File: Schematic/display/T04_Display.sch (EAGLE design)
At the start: 46 parts

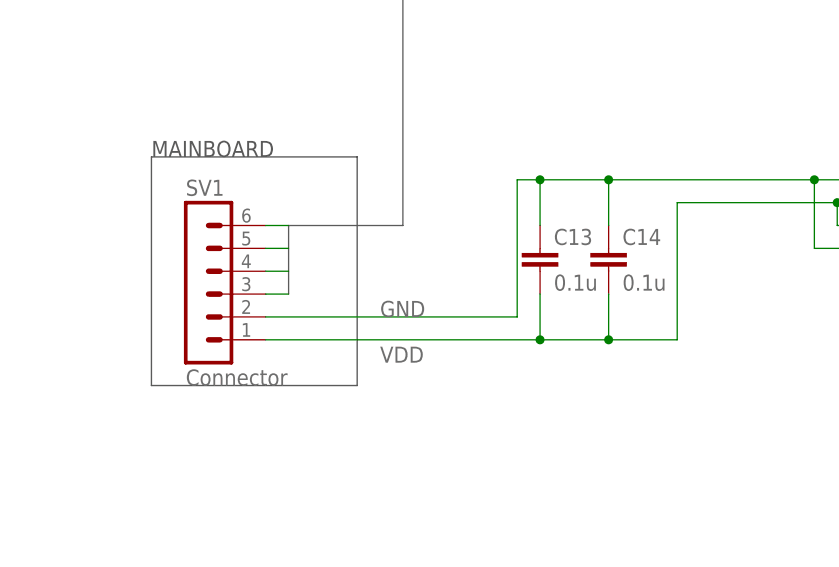
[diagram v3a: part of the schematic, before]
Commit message: Mainboard & Display layout updates - Molex connectors, Mounting Holes, Greenberg Email Additions
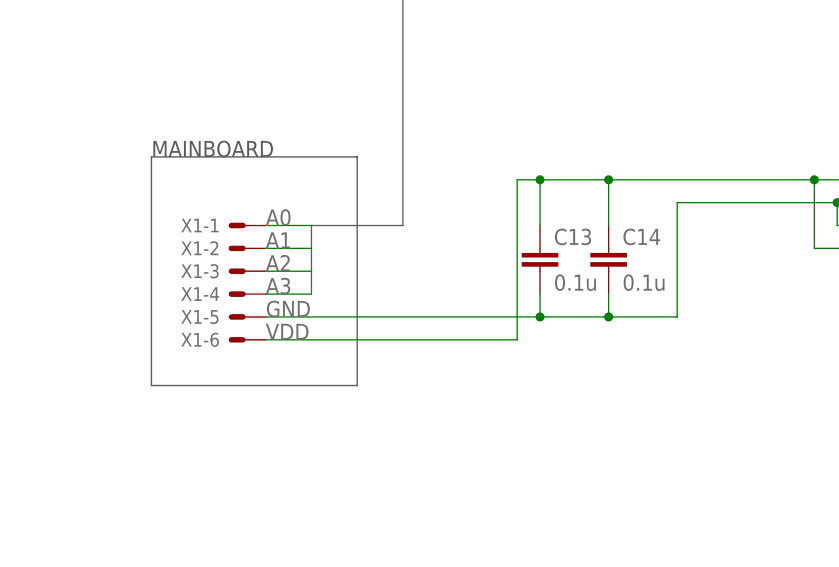
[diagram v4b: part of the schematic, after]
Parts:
- removed SV1: Connector, con-lstb:MA06-1
- added X1: (no value), con-molex:22-23-2061
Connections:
- net A0: now also X1-1.S; no longer SV1.6
- net A1: now also X1-2.S; no longer SV1.5
- net A2: now also X1-3.S; no longer SV1.4
- net A3: now also X1-4.S; no longer SV1.3
- net GND: now also X1-6.S; no longer SV1.2
- net VDD: now also X1-5.S; no longer SV1.1
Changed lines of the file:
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@@
 <parts>
 <part name="FRAME1" library="frames" deviceset="FRAME_B_L" device=""/>
-<part name="SV1" library="con-lstb" deviceset="MA06-1" device="" value="Connector"/>
 <part name="U$1" library="display" deviceset="2N7002" device=""/>
 <part name="REAR" library="display" deviceset="CD4043" device=""/>
@@
 <part name="R8" library="rcl" deviceset="R-US_" device="R1206" value="150"/>
 <part name="R9" library="rcl" deviceset="R-US_" device="R1206" value="150"/>
+<part name="X1" library="con-molex" deviceset="22-23-2061" device=""/>
 </parts>
 <sheets>
@@
 <instance part="FRAME1" gate="G$1" x="0" y="0"/>
 <instance part="FRAME1" gate="G$2" x="325.12" y="0"/>
-<instance part="SV1" gate="1" x="55.88" y="63.5"/>
 <instance part="U$1" gate="G$1" x="299.72" y="248.92"/>
 <instance part="REAR" gate="G$1" x="254" y="200.66"/>
@@
 <instance part="R8" gate="G$1" x="335.28" y="124.46" rot="R90"/>
 <instance part="R9" gate="G$1" x="299.72" y="124.46" rot="R90"/>
+<instance part="X1" gate="-1" x="60.96" y="68.58" rot="MR0"/>
+<instance part="X1" gate="-2" x="60.96" y="66.04" rot="MR0"/>
+<instance part="X1" gate="-3" x="60.96" y="63.5" rot="MR0"/>
+<instance part="X1" gate="-4" x="60.96" y="60.96" rot="MR0"/>
+<instance part="X1" gate="-5" x="60.96" y="58.42" rot="MR0"/>
+<instance part="X1" gate="-6" x="60.96" y="55.88" rot="MR0"/>
 </instances>
 <busses>
@@
 <bus name="A0,A1,A2,A3">
 <segment>
-<wire x1="66.04" y1="60.96" x2="66.04" y2="68.58" width="0.762" layer="92"/>
-<wire x1="66.04" y1="68.58" x2="78.74" y2="68.58" width="0.762" layer="92"/>
+<wire x1="68.58" y1="60.96" x2="68.58" y2="68.58" width="0.762" layer="92"/>
+<wire x1="68.58" y1="68.58" x2="78.74" y2="68.58" width="0.762" layer="92"/>
 <wire x1="78.74" y1="68.58" x2="78.74" y2="99.06" width="0.762" layer="92"/>
 <wire x1="78.74" y1="99.06" x2="127" y2="99.06" width="0.762" layer="92"/>
@@
 </segment>
 <segment>
-<pinref part="SV1" gate="1" pin="2"/>
-<wire x1="63.5" y1="58.42" x2="91.44" y2="58.42" width="0.1524" layer="91"/>
-<wire x1="91.44" y1="58.42" x2="91.44" y2="73.66" width="0.1524" layer="91"/>
+<wire x1="91.44" y1="55.88" x2="91.44" y2="73.66" width="0.1524" layer="91"/>
 <pinref part="U$3" gate="G$1" pin="VSS"/>
 <wire x1="91.44" y1="73.66" x2="93.98" y2="73.66" width="0.1524" layer="91"/>
-<label x="76.2" y="58.42" size="1.778" layer="95"/>
+<label x="63.5" y="58.42" size="1.778" layer="95"/>
 <junction x="124.46" y="73.66"/>
 <wire x1="93.98" y1="73.66" x2="101.6" y2="73.66" width="0.1524" layer="91"/>
@@
 <wire x1="101.6" y1="68.58" x2="101.6" y2="73.66" width="0.1524" layer="91"/>
 <junction x="101.6" y="73.66"/>
+<pinref part="X1" gate="-6" pin="S"/>
+<wire x1="91.44" y1="55.88" x2="63.5" y2="55.88" width="0.1524" layer="91"/>
 </segment>
 </net>
@@
 </segment>
 <segment>
-<pinref part="SV1" gate="1" pin="1"/>
-<wire x1="63.5" y1="55.88" x2="93.98" y2="55.88" width="0.1524" layer="91"/>
-<wire x1="93.98" y1="55.88" x2="101.6" y2="55.88" width="0.1524" layer="91"/>
-<wire x1="101.6" y1="55.88" x2="109.22" y2="55.88" width="0.1524" layer="91"/>
-<wire x1="109.22" y1="55.88" x2="109.22" y2="71.12" width="0.1524" layer="91"/>
+<wire x1="93.98" y1="58.42" x2="101.6" y2="58.42" width="0.1524" layer="91"/>
+<wire x1="101.6" y1="58.42" x2="109.22" y2="58.42" width="0.1524" layer="91"/>
+<wire x1="109.22" y1="58.42" x2="109.22" y2="71.12" width="0.1524" layer="91"/>
 <pinref part="U$3" gate="G$1" pin="VDD"/>
 <wire x1="109.22" y1="71.12" x2="127" y2="71.12" width="0.1524" layer="91"/>
-<label x="76.2" y="53.34" size="1.778" layer="95"/>
+<label x="63.5" y="55.88" size="1.778" layer="95"/>
 <junction x="127" y="71.12"/>
 <wire x1="127" y1="71.12" x2="129.54" y2="71.12" width="0.1524" layer="91"/>
@@
 <wire x1="129.54" y1="68.58" x2="127" y2="68.58" width="0.1524" layer="91"/>
 <wire x1="127" y1="68.58" x2="127" y2="71.12" width="0.1524" layer="91"/>
-<junction x="93.98" y="55.88"/>
-<junction x="101.6" y="55.88"/>
+<junction x="101.6" y="58.42"/>
 <pinref part="C13" gate="G$1" pin="2"/>
-<wire x1="93.98" y1="60.96" x2="93.98" y2="55.88" width="0.1524" layer="91"/>
+<wire x1="93.98" y1="60.96" x2="93.98" y2="58.42" width="0.1524" layer="91"/>
 <pinref part="C14" gate="G$1" pin="2"/>
-<wire x1="101.6" y1="60.96" x2="101.6" y2="55.88" width="0.1524" layer="91"/>
+<wire x1="101.6" y1="60.96" x2="101.6" y2="58.42" width="0.1524" layer="91"/>
+<pinref part="X1" gate="-5" pin="S"/>
+<wire x1="93.98" y1="58.42" x2="63.5" y2="58.42" width="0.1524" layer="91"/>
+<junction x="93.98" y="58.42"/>
 </segment>
 </net>
@@
 </segment>
 <segment>
-<pinref part="SV1" gate="1" pin="6"/>
-<wire x1="66.04" y1="68.58" x2="63.5" y2="68.58" width="0.1524" layer="91"/>
+<wire x1="68.58" y1="68.58" x2="63.5" y2="68.58" width="0.1524" layer="91"/>
+<pinref part="X1" gate="-1" pin="S"/>
+<label x="63.5" y="68.58" size="1.778" layer="95"/>
 </segment>
 </net>
@@
 </segment>
 <segment>
-<pinref part="SV1" gate="1" pin="5"/>
-<wire x1="66.04" y1="66.04" x2="63.5" y2="66.04" width="0.1524" layer="91"/>
+<wire x1="68.58" y1="66.04" x2="63.5" y2="66.04" width="0.1524" layer="91"/>
+<pinref part="X1" gate="-2" pin="S"/>
+<label x="63.5" y="66.04" size="1.778" layer="95"/>
 </segment>
 </net>
@@
 </segment>
 <segment>
-<pinref part="SV1" gate="1" pin="4"/>
-<wire x1="66.04" y1="63.5" x2="63.5" y2="63.5" width="0.1524" layer="91"/>
+<wire x1="68.58" y1="63.5" x2="63.5" y2="63.5" width="0.1524" layer="91"/>
+<pinref part="X1" gate="-3" pin="S"/>
+<label x="63.5" y="63.5" size="1.778" layer="95"/>
 </segment>
 </net>
@@
 </segment>
 <segment>
-<pinref part="SV1" gate="1" pin="3"/>
-<wire x1="66.04" y1="60.96" x2="63.5" y2="60.96" width="0.1524" layer="91"/>
-</segment>
-</net>
+<wire x1="68.58" y1="60.96" x2="63.5" y2="60.96" width="0.1524" layer="91"/>
+<pinref part="X1" gate="-4" pin="S"/>
+<label x="63.5" y="60.96" size="1.778" layer="95"/>
+</segment>
+</net>

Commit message: Updated Schematic and Revision text to match instructor review.
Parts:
- removed C14: 0.1u, resistor:C-EUC1206
- added R10, R11, R12, R13, R14, R15, R16, R17, R18, R19, R20, R21: 4700, rcl:R-US_R1206
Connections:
- removed net N$11: R7.2, U$9.S
- removed net N$2: R8.2, U$8.S
- removed net N$7: R9.2, U$6.S
- new net N$21: LED6.C, U$9.D
- new net N$22: LED4.C, U$6.D
- new net N$23: LED5.C, U$8.D
- net BRES: now also R18.2
- net BS1: now also R21.2
- net BS2: now also R20.2
- net BS3: now also R19.2
- net GND: now also R10.1, R11.1, R12.1, R13.1, R14.1, R15.1, R16.1, R17.1, R18.1, R19.1, R20.1, R21.1, U$1.S, U$10.S, U$12.S, U$13.S, U$4.S, U$5.S, U$6.S, U$8.S, U$9.S; no longer C14.1, LED1.C, LED2.C, LED3.C, LED4.C, LED5.C, LED6.C, LED7.C, LED8.C, LED9.C
- net LRES: now also R14.2
- net LS1: now also R17.2
- net LS2: now also R16.2
- net LS3: now also R15.2
- net N$1: now also LED3.C, U$5.D; no longer R5.2, U$4.S
- net N$13: now also LED7.C, U$10.D; no longer R1.2, U$10.S
- net N$15: now also LED8.C, U$12.D; no longer R2.2, U$12.S
- net N$17: now also LED9.C, U$13.D; no longer R3.2, U$13.S
- net N$3: now also LED2.C, U$4.D; no longer R6.2, U$5.S
- net N$4: now also LED1.C, U$1.D; no longer R4.2, U$1.S
- net RRES: now also R13.2
- net RS1: now also R10.2
- net RS2: now also R11.2
- net RS3: now also R12.2
- net VDD: now also R1.2, R2.2, R3.2, R4.2, R5.2, R6.2, R7.2, R8.2, R9.2; no longer C14.2, U$1.D, U$10.D, U$12.D, U$13.D, U$4.D, U$5.D, U$6.D, U$8.D, U$9.D
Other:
- note added: "1.2"
- note removed: "1.1"
- moved on the sheet: LED1, LED2, LED3, LED4, LED5, LED6, LED7, LED8, LED9, R1, R2, R3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

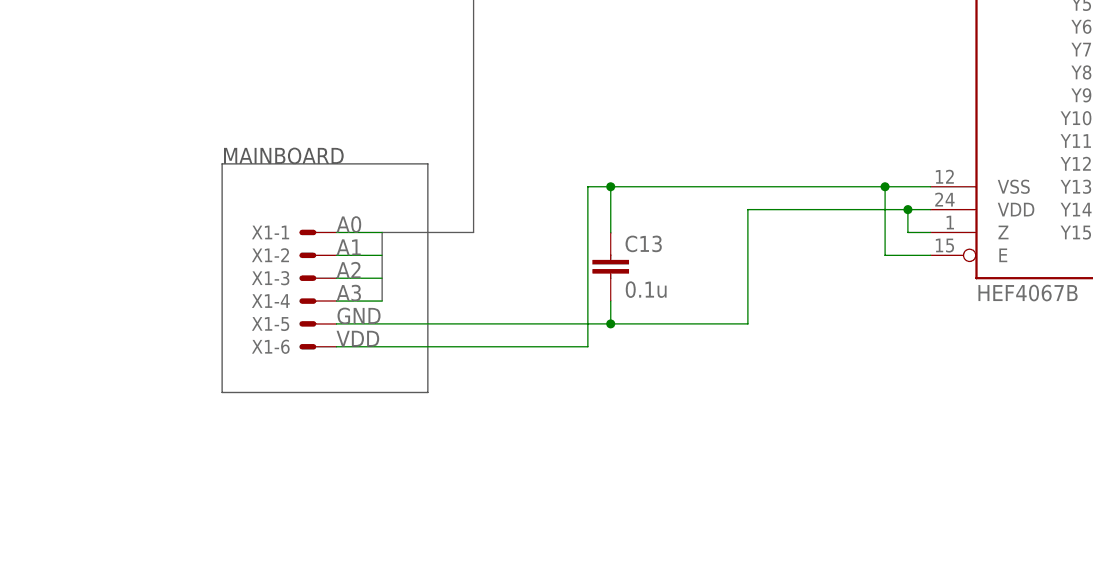
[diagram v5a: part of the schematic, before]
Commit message: Display w/ 7-pin molex
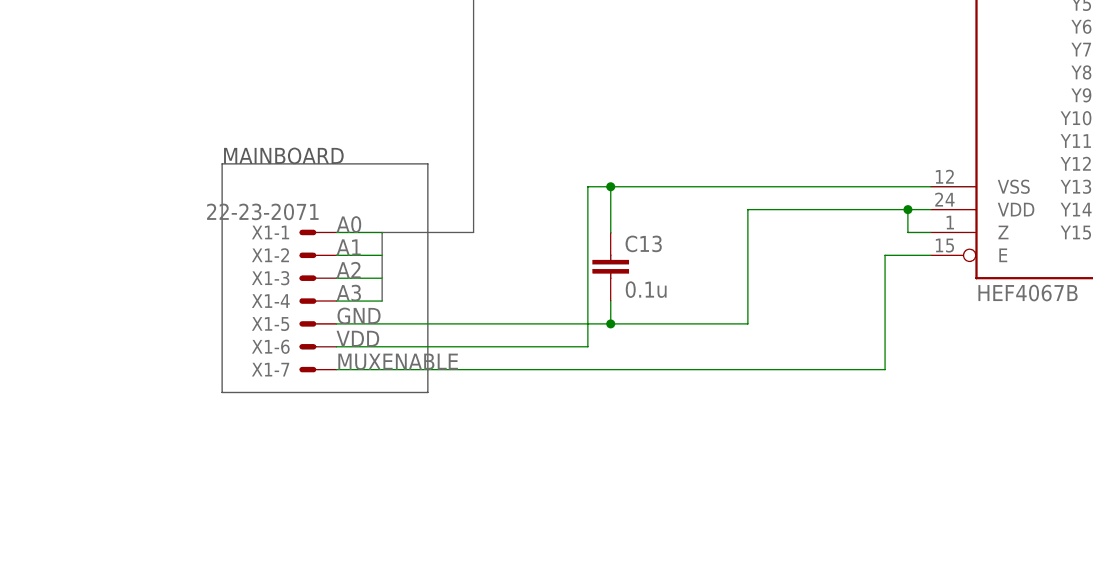
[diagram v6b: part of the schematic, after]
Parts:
- X1: value (none) -> 22-23-2071; device con-molex:22-23-2061 -> con-molex:22-23-2071
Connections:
- new net MUXENABLE: U$3.E, X1-7.S
- net GND: no longer U$3.E
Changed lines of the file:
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@@
 <?xml version="1.0" encoding="utf-8"?>
 <!DOCTYPE eagle SYSTEM "eagle.dtd">
-<eagle version="6.3">
+<eagle version="7.1.0">
 <drawing>
 <settings>
@@
 <part name="R8" library="rcl" deviceset="R-US_" device="R1206" value="150"/>
 <part name="R9" library="rcl" deviceset="R-US_" device="R1206" value="150"/>
-<part name="X1" library="con-molex" deviceset="22-23-2061" device=""/>
 <part name="R10" library="rcl" deviceset="R-US_" device="R1206" value="4700"/>
 <part name="R11" library="rcl" deviceset="R-US_" device="R1206" value="4700"/>
@@
 <part name="R20" library="rcl" deviceset="R-US_" device="R1206" value="4700"/>
 <part name="R21" library="rcl" deviceset="R-US_" device="R1206" value="4700"/>
+<part name="X1" library="con-molex" deviceset="22-23-2071" device=""/>
 </parts>
 <sheets>
@@
 <instance part="R8" gate="G$1" x="335.28" y="137.16" rot="R90"/>
 <instance part="R9" gate="G$1" x="299.72" y="137.16" rot="R90"/>
-<instance part="X1" gate="-1" x="60.96" y="68.58" rot="MR0"/>
-<instance part="X1" gate="-2" x="60.96" y="66.04" rot="MR0"/>
-<instance part="X1" gate="-3" x="60.96" y="63.5" rot="MR0"/>
-<instance part="X1" gate="-4" x="60.96" y="60.96" rot="MR0"/>
-<instance part="X1" gate="-5" x="60.96" y="58.42" rot="MR0"/>
-<instance part="X1" gate="-6" x="60.96" y="55.88" rot="MR0"/>
 <instance part="R10" gate="G$1" x="177.8" y="66.04" rot="R90"/>
 <instance part="R11" gate="G$1" x="185.42" y="66.04" rot="R90"/>
@@
 <instance part="R20" gate="G$1" x="101.6" y="139.7" rot="R90"/>
 <instance part="R21" gate="G$1" x="109.22" y="139.7" rot="R90"/>
+<instance part="X1" gate="-1" x="60.96" y="68.58" rot="MR0"/>
+<instance part="X1" gate="-2" x="60.96" y="66.04" rot="MR0"/>
+<instance part="X1" gate="-3" x="60.96" y="63.5" rot="MR0"/>
+<instance part="X1" gate="-4" x="60.96" y="60.96" rot="MR0"/>
+<instance part="X1" gate="-5" x="60.96" y="58.42" rot="MR0"/>
+<instance part="X1" gate="-6" x="60.96" y="55.88" rot="MR0"/>
+<instance part="X1" gate="-7" x="60.96" y="53.34" rot="MR0"/>
 </instances>
 <busses>
@@
 <wire x1="91.44" y1="73.66" x2="93.98" y2="73.66" width="0.1524" layer="91"/>
 <label x="63.5" y="58.42" size="1.778" layer="95"/>
-<junction x="124.46" y="73.66"/>
-<wire x1="93.98" y1="73.66" x2="124.46" y2="73.66" width="0.1524" layer="91"/>
-<wire x1="124.46" y1="73.66" x2="129.54" y2="73.66" width="0.1524" layer="91"/>
-<pinref part="U$3" gate="G$1" pin="E"/>
-<wire x1="129.54" y1="66.04" x2="124.46" y2="66.04" width="0.1524" layer="91"/>
-<wire x1="124.46" y1="66.04" x2="124.46" y2="73.66" width="0.1524" layer="91"/>
+<wire x1="93.98" y1="73.66" x2="129.54" y2="73.66" width="0.1524" layer="91"/>
 <pinref part="C13" gate="G$1" pin="1"/>
 <wire x1="93.98" y1="68.58" x2="93.98" y2="73.66" width="0.1524" layer="91"/>
 <junction x="93.98" y="73.66"/>
+<wire x1="91.44" y1="55.88" x2="63.5" y2="55.88" width="0.1524" layer="91"/>
 <pinref part="X1" gate="-6" pin="S"/>
-<wire x1="91.44" y1="55.88" x2="63.5" y2="55.88" width="0.1524" layer="91"/>
 </segment>
 <segment>
@@
 <pinref part="C13" gate="G$1" pin="2"/>
 <wire x1="93.98" y1="60.96" x2="93.98" y2="58.42" width="0.1524" layer="91"/>
-<pinref part="X1" gate="-5" pin="S"/>
 <wire x1="93.98" y1="58.42" x2="63.5" y2="58.42" width="0.1524" layer="91"/>
 <junction x="93.98" y="58.42"/>
+<pinref part="X1" gate="-5" pin="S"/>
 </segment>
 <segment>
@@
 <segment>
 <wire x1="68.58" y1="68.58" x2="63.5" y2="68.58" width="0.1524" layer="91"/>
+<label x="63.5" y="68.58" size="1.778" layer="95"/>
 <pinref part="X1" gate="-1" pin="S"/>
-<label x="63.5" y="68.58" size="1.778" layer="95"/>
 </segment>
 </net>
@@
 <segment>
 <wire x1="68.58" y1="66.04" x2="63.5" y2="66.04" width="0.1524" layer="91"/>
+<label x="63.5" y="66.04" size="1.778" layer="95"/>
 <pinref part="X1" gate="-2" pin="S"/>
-<label x="63.5" y="66.04" size="1.778" layer="95"/>
 </segment>
 </net>
@@
 <segment>
 <wire x1="68.58" y1="63.5" x2="63.5" y2="63.5" width="0.1524" layer="91"/>
+<label x="63.5" y="63.5" size="1.778" layer="95"/>
 <pinref part="X1" gate="-3" pin="S"/>
-<label x="63.5" y="63.5" size="1.778" layer="95"/>
 </segment>
 </net>
@@
 <segment>
 <wire x1="68.58" y1="60.96" x2="63.5" y2="60.96" width="0.1524" layer="91"/>
+<label x="63.5" y="60.96" size="1.778" layer="95"/>
 <pinref part="X1" gate="-4" pin="S"/>
-<label x="63.5" y="60.96" size="1.778" layer="95"/>
 </segment>
 </net>
@@
 </segment>
 </net>
+<net name="MUXENABLE" class="0">
+<segment>
+<pinref part="U$3" gate="G$1" pin="E"/>
+<wire x1="129.54" y1="66.04" x2="124.46" y2="66.04" width="0.1524" layer="91"/>
+<wire x1="124.46" y1="53.34" x2="124.46" y2="66.04" width="0.1524" layer="91"/>
+<pinref part="X1" gate="-7" pin="S"/>
+<wire x1="63.5" y1="53.34" x2="124.46" y2="53.34" width="0.1524" layer="91"/>
+<label x="63.5" y="53.34" size="1.778" layer="95"/>
+</segment>
+</net>
